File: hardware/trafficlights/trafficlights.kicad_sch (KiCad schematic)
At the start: 3 parts, among them Q1 Q_NMOS_SGD

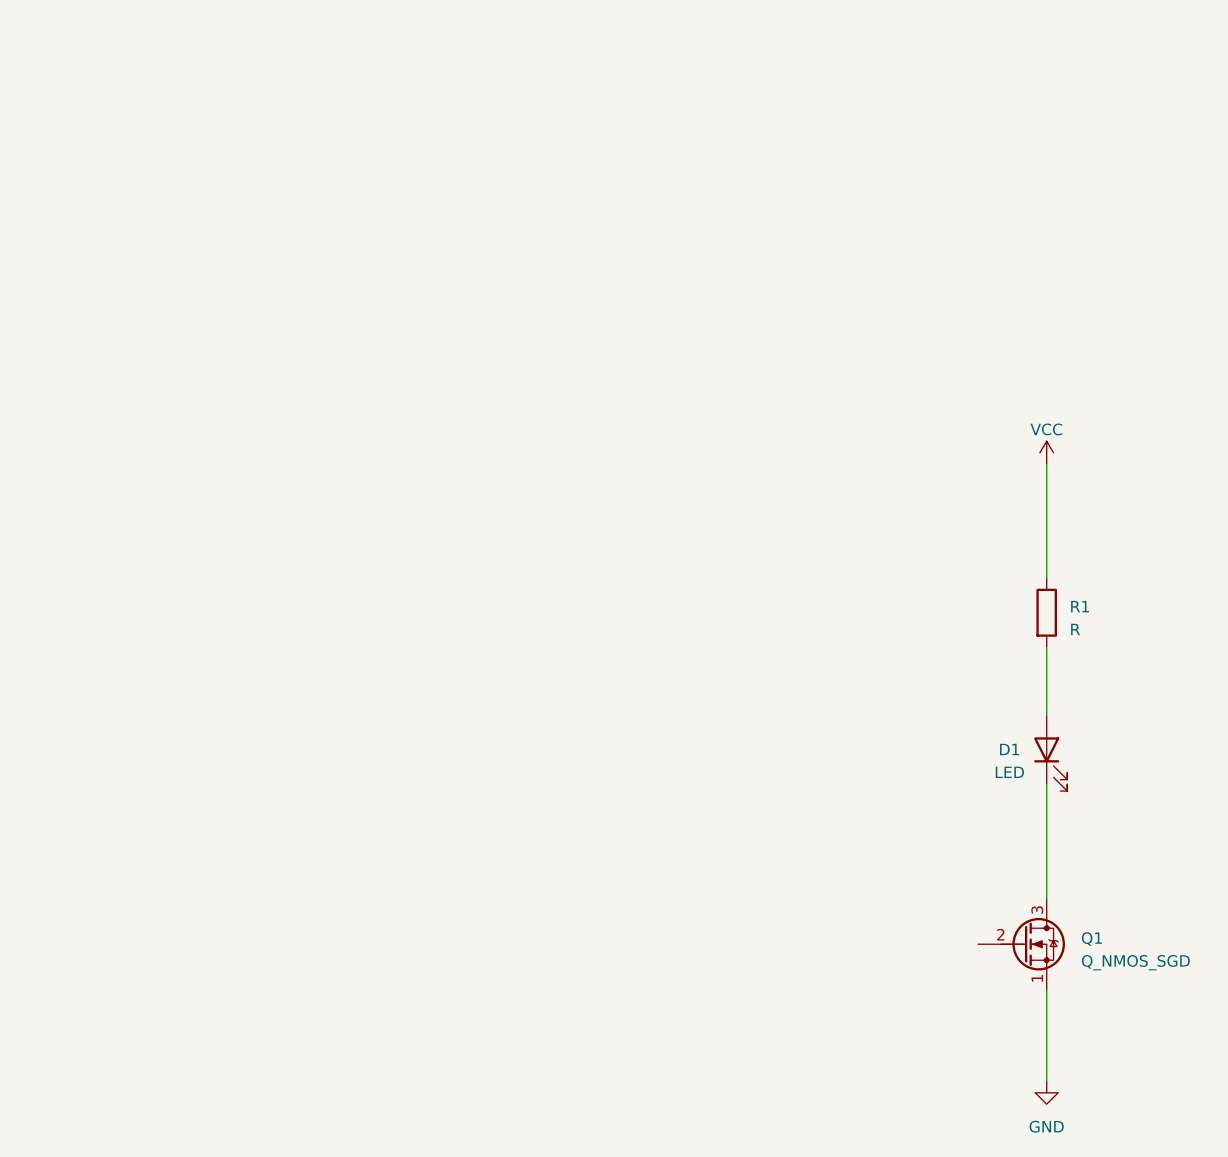
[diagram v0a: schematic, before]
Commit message: Made PCB design for perforated board.
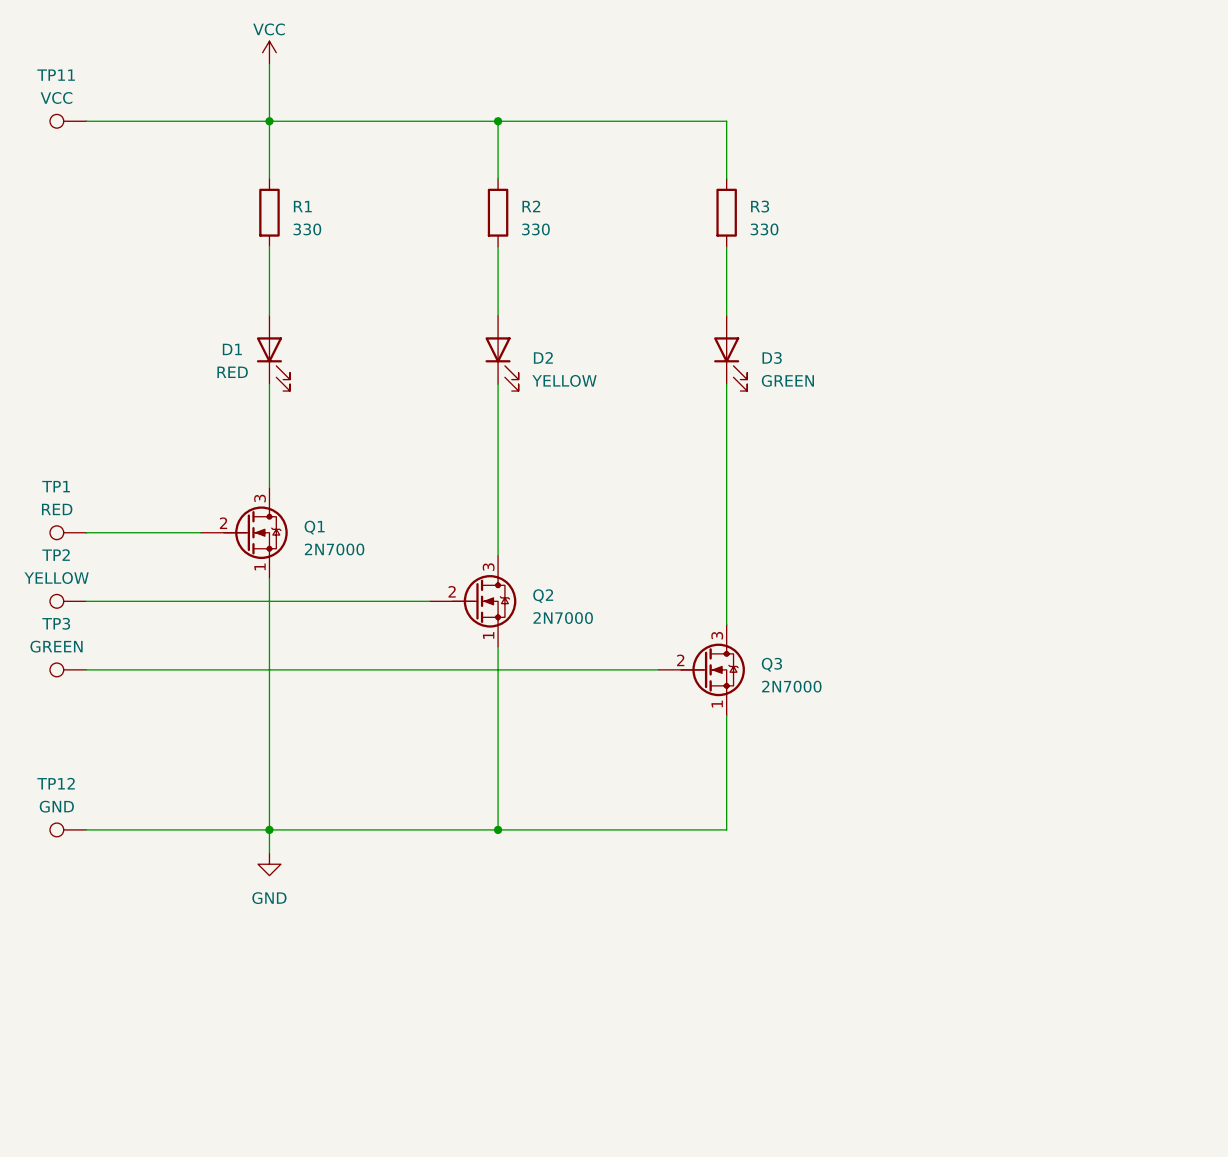
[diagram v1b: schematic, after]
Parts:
- added D2: YELLOW, LED_THT:LED_D5.0mm, symbol Device:LED
- added D3: GREEN, LED_THT:LED_D5.0mm, symbol Device:LED
- added Q2, Q3: 2N7000, Package_TO_SOT_THT:TO-92_Inline_Wide, symbol Device:Q_NMOS_SGD
- added R2, R3: 330, Resistor_THT:R_Axial_DIN0414_L11.9mm_D4.5mm_P15.24mm_Horizontal, symbol Device:R
- added TP1: RED, Connector_Wire:SolderWire-0.1sqmm_1x01_D0.4mm_OD1mm, symbol Connector:TestPoint
- added TP11: VCC, Connector_Wire:SolderWire-0.1sqmm_1x01_D0.4mm_OD1mm, symbol Connector:TestPoint
- added TP12: GND, Connector_Wire:SolderWire-0.1sqmm_1x01_D0.4mm_OD1mm, symbol Connector:TestPoint
- added TP2: YELLOW, Connector_Wire:SolderWire-0.1sqmm_1x01_D0.4mm_OD1mm, symbol Connector:TestPoint
- added TP3: GREEN, Connector_Wire:SolderWire-0.1sqmm_1x01_D0.4mm_OD1mm, symbol Connector:TestPoint
- D1: value LED -> RED; footprint (none) -> LED_THT:LED_D5.0mm
- Q1: value Q_NMOS_SGD -> 2N7000; footprint (none) -> Package_TO_SOT_THT:TO-92_Inline_Wide
- R1: value R -> 330; footprint (none) -> Resistor_THT:R_Axial_DIN0414_L11.9mm_D4.5mm_P15.24mm_Horizontal
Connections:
- net GND: now also Q2.1 (S), Q3.1 (S), TP12.1
- net VCC: now also R2.1, R3.1, TP11.1
- net at Q1.2 (G): now also TP1.1
- new net: D3.1 (K), Q3.3 (D)
- new net: D3.2 (A), R3.2
- new net: D2.1 (K), Q2.3 (D)
- new net: D2.2 (A), R2.2
- new net: Q3.2 (G), TP3.1
- new net: Q2.2 (G), TP2.1
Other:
- moved on the sheet: D1, Q1, R1
